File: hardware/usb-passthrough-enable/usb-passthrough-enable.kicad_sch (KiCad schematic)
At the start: 10 parts, among them J1 Conn_02x04_Odd_Even, J2 USB_A, J3 USB_B, Q1 KSP43BU, U1 Omron_G3VM-61A1

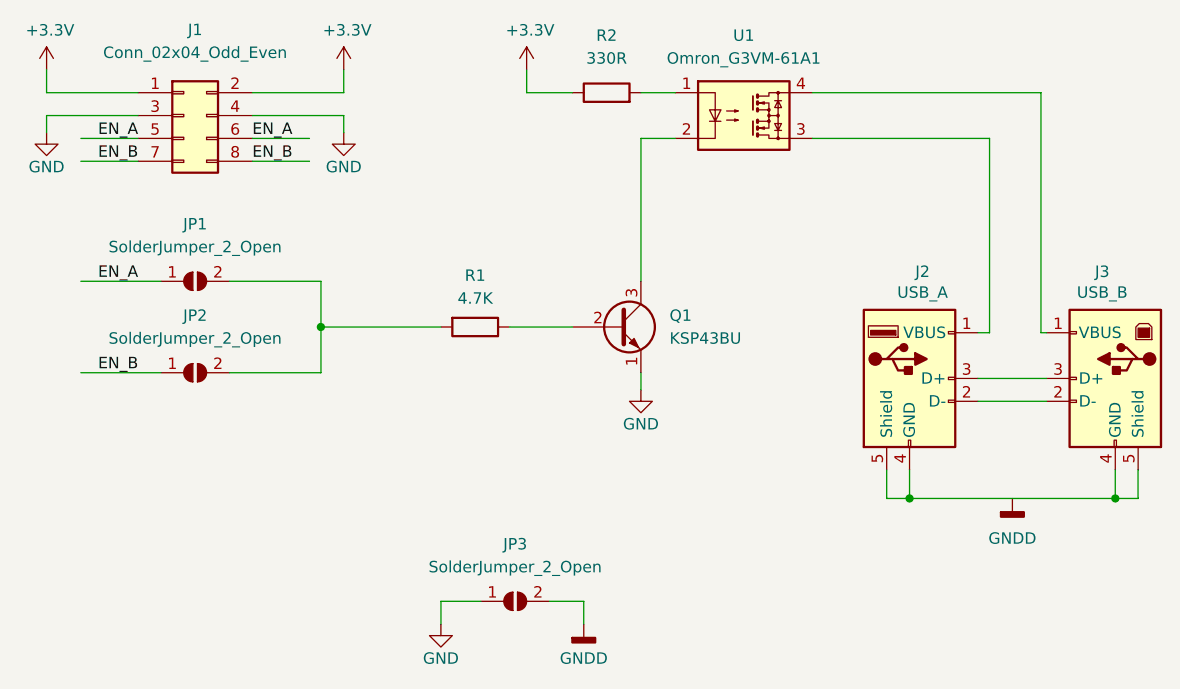
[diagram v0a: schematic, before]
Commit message: Rev B USB switching PCB
Correct error in ground plane
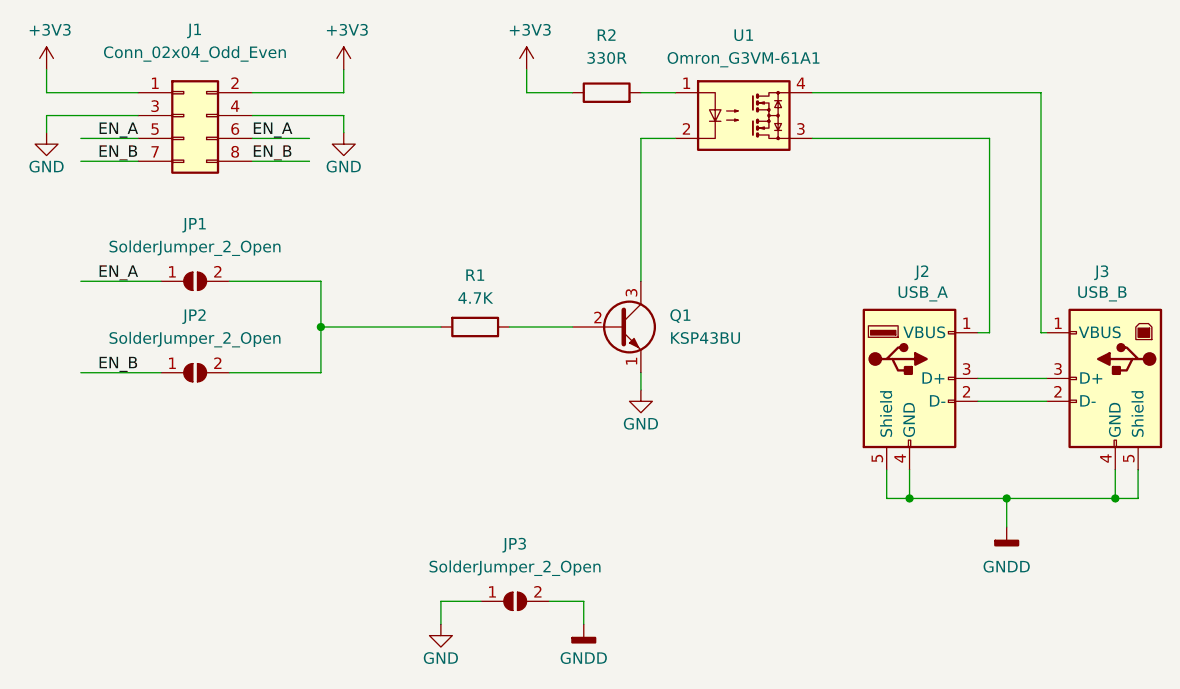
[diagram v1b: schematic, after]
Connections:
- net GNDD: now also J2.4 (GND), J2.5 (Shield), J3.4 (GND), J3.5 (Shield)
